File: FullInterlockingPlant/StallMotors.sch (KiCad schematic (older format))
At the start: 41 parts

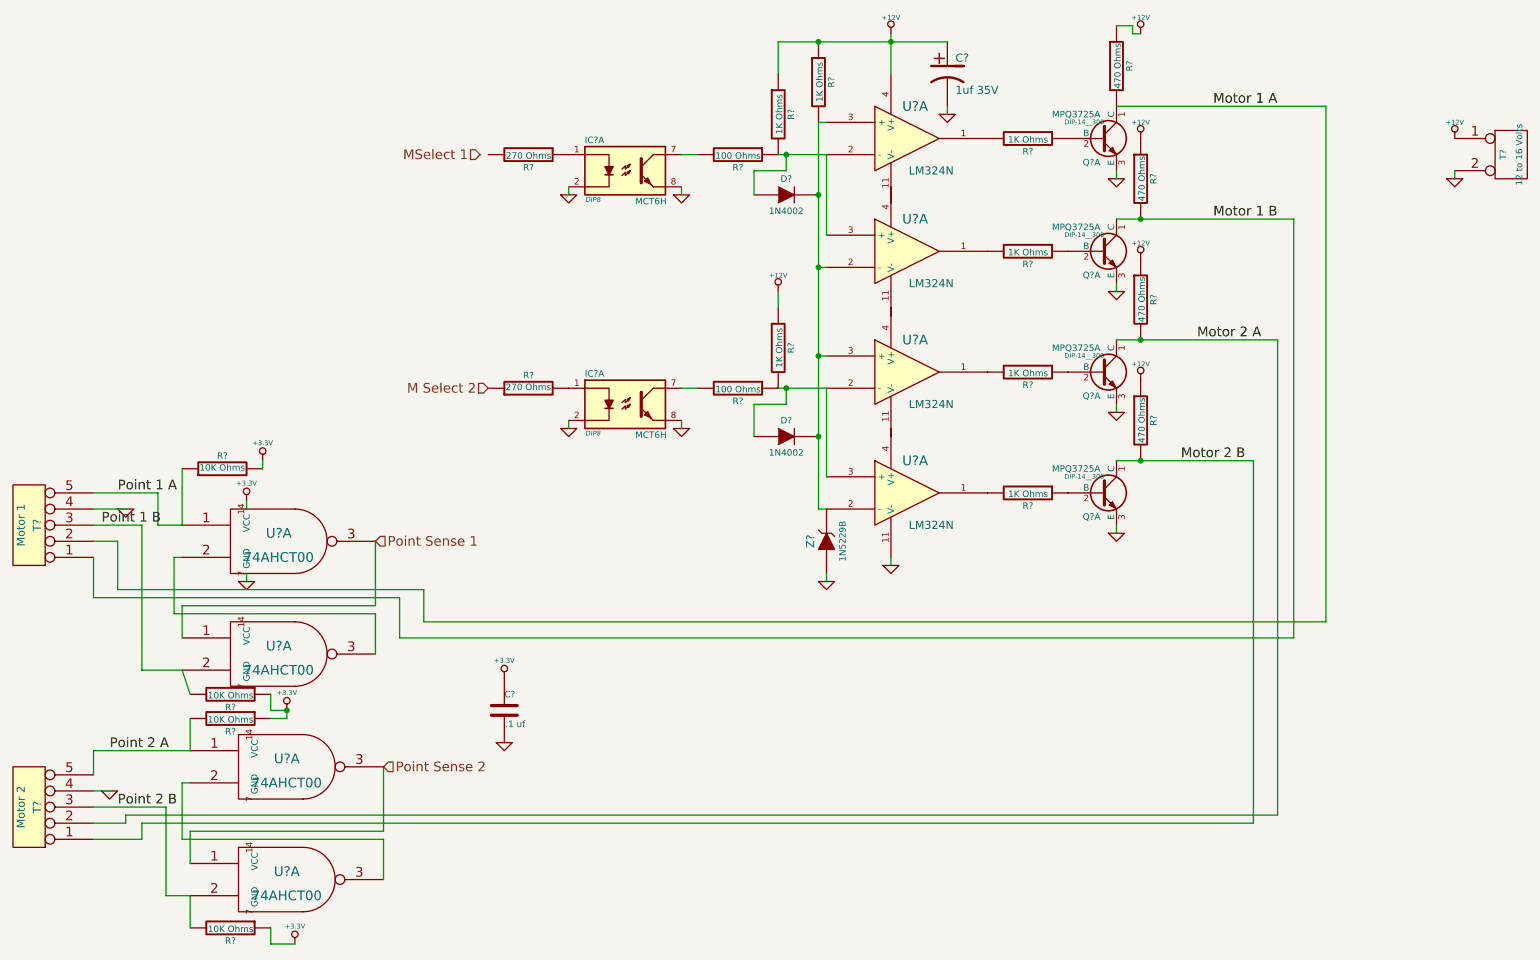
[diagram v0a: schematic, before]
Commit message: Complete FullInterlockingPlant (without CAN)
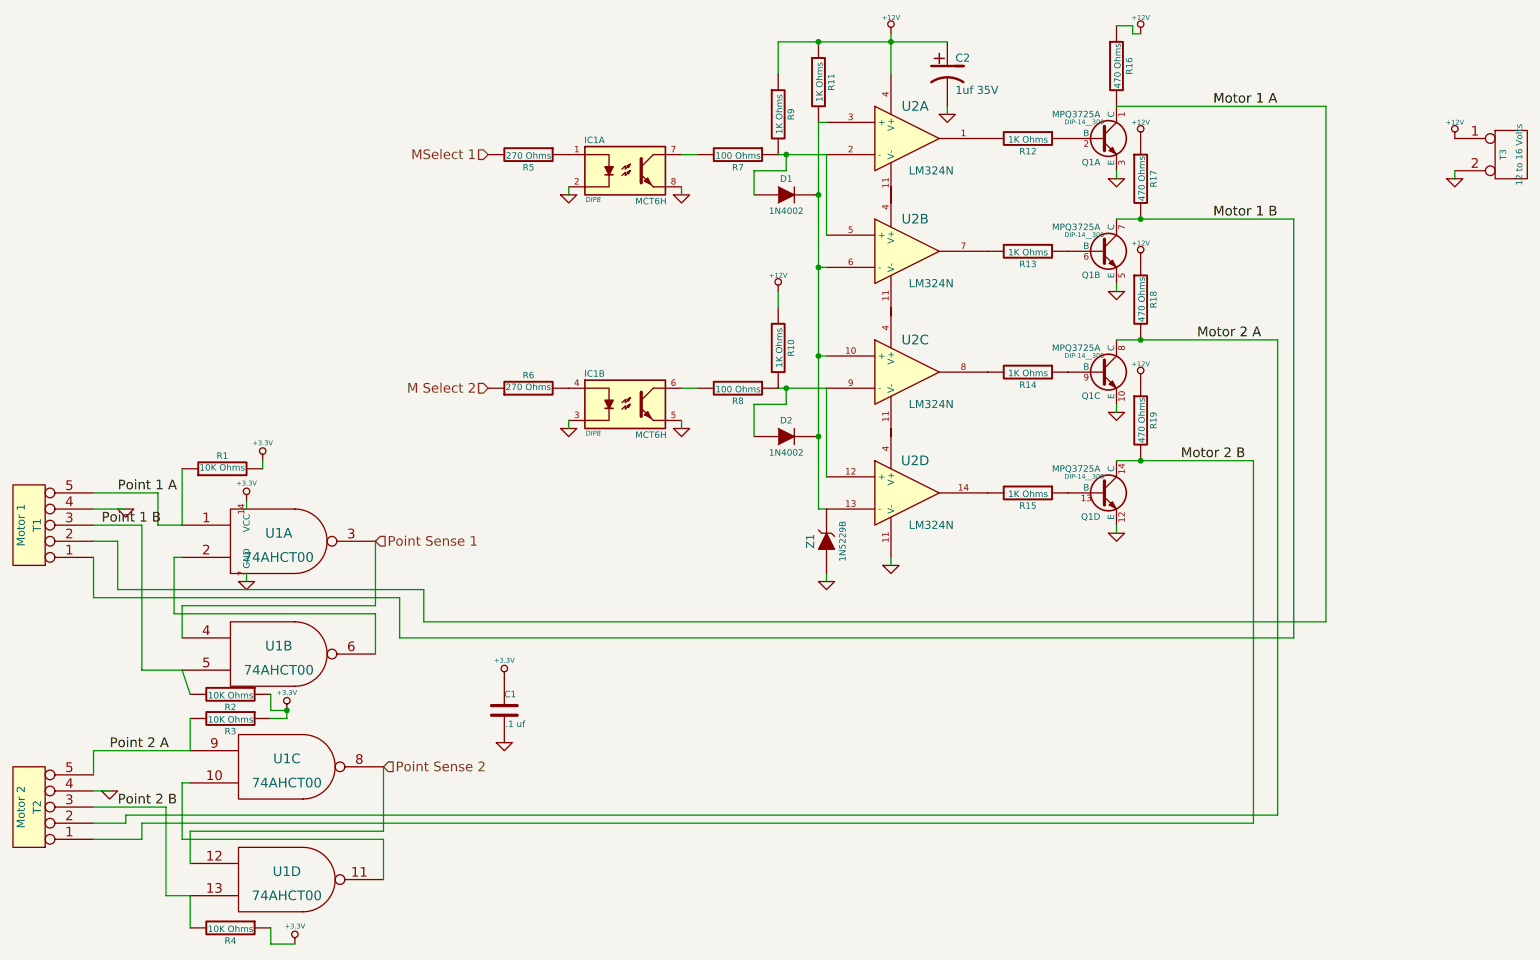
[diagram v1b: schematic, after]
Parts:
- gave numbers to parts that had none: 31
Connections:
- net GND: now also IC1.3, IC1.5, Q1.10 (E), Q1.12 (E), Q1.5 (E); no longer IC1.2, IC1.8, Q1.3 (E), Q1.3 (E), Q1.3 (E)
- net MSelect 1: now also R5.2
- net Motor 1 B: now also Q1.7 (C); no longer Q1.1 (C)
- net Motor 2 A: now also Q1.8 (C); no longer Q1.1 (C)
- net Motor 2 B: now also Q1.14 (C); no longer Q1.1 (C)
- net Point 1 B: now also U1.5; no longer U1.2
- net Point 2 A: now also U1.9; no longer U1.1
- net Point 2 B: now also U1.13; no longer U1.2
- net Point Sense 1: now also U1.4; no longer U1.1
- net Point Sense 2: now also U1.12, U1.8; no longer U1.1, U1.3
- net at U1.2: now also U1.6; no longer U1.3
- net at R6.2: now also IC1.4; no longer IC1.1
- net at R8.2: now also IC1.6; no longer IC1.7
- net at D1.1 (A), R7.1, R9.2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: now also U2.5 (+); no longer U2.3 (+)
- net at D1.2 (K), D2.2 (K), R11.2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: now also U2.10 (+), U2.13 (-), U2.6 (-); no longer U2.2 (-), U2.2 (-), U2.3 (+)
- net at R13.2: now also U2.7; no longer U2.1
- net at R14.2: now also U2.8; no longer U2.1
- net at D2.1 (A), R10.2, R8.1: now also U2.12 (+), U2.9 (-); no longer U2.2 (-), U2.3 (+)
- net at R15.2: now also U2.14; no longer U2.1
- net at R13.1: now also Q1.6 (B); no longer Q1.2 (B)
- net at R14.1: now also Q1.9 (B); no longer Q1.2 (B)
- net at R15.1: now also Q1.13 (B); no longer Q1.2 (B)
- new net: U1.10, U1.11
